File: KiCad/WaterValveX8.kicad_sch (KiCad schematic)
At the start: 89 parts, among them J10 Screw_Terminal_01x03, J2 Conn_01x03_Male, J3 Screw_Terminal_01x02, J4 Conn_01x01_Male, J5 Screw_Terminal_01x03, J6 Conn_01x04_Male, J7 Screw_Terminal_01x03, J8 Screw_Terminal_01x03, J9 Screw_Terminal_01x03, Q1 IRLML2502, Q2 IRLML2502, Q3 IRLML2502, Q4 IRLML2502, Q5 IRLML2502, Q6 IRLML2502, Q7 IRLML2502, Q8 IRLML2502, U1 L7805, U2 XIAO-ESP32-C6-SMD, U3 MT2499A

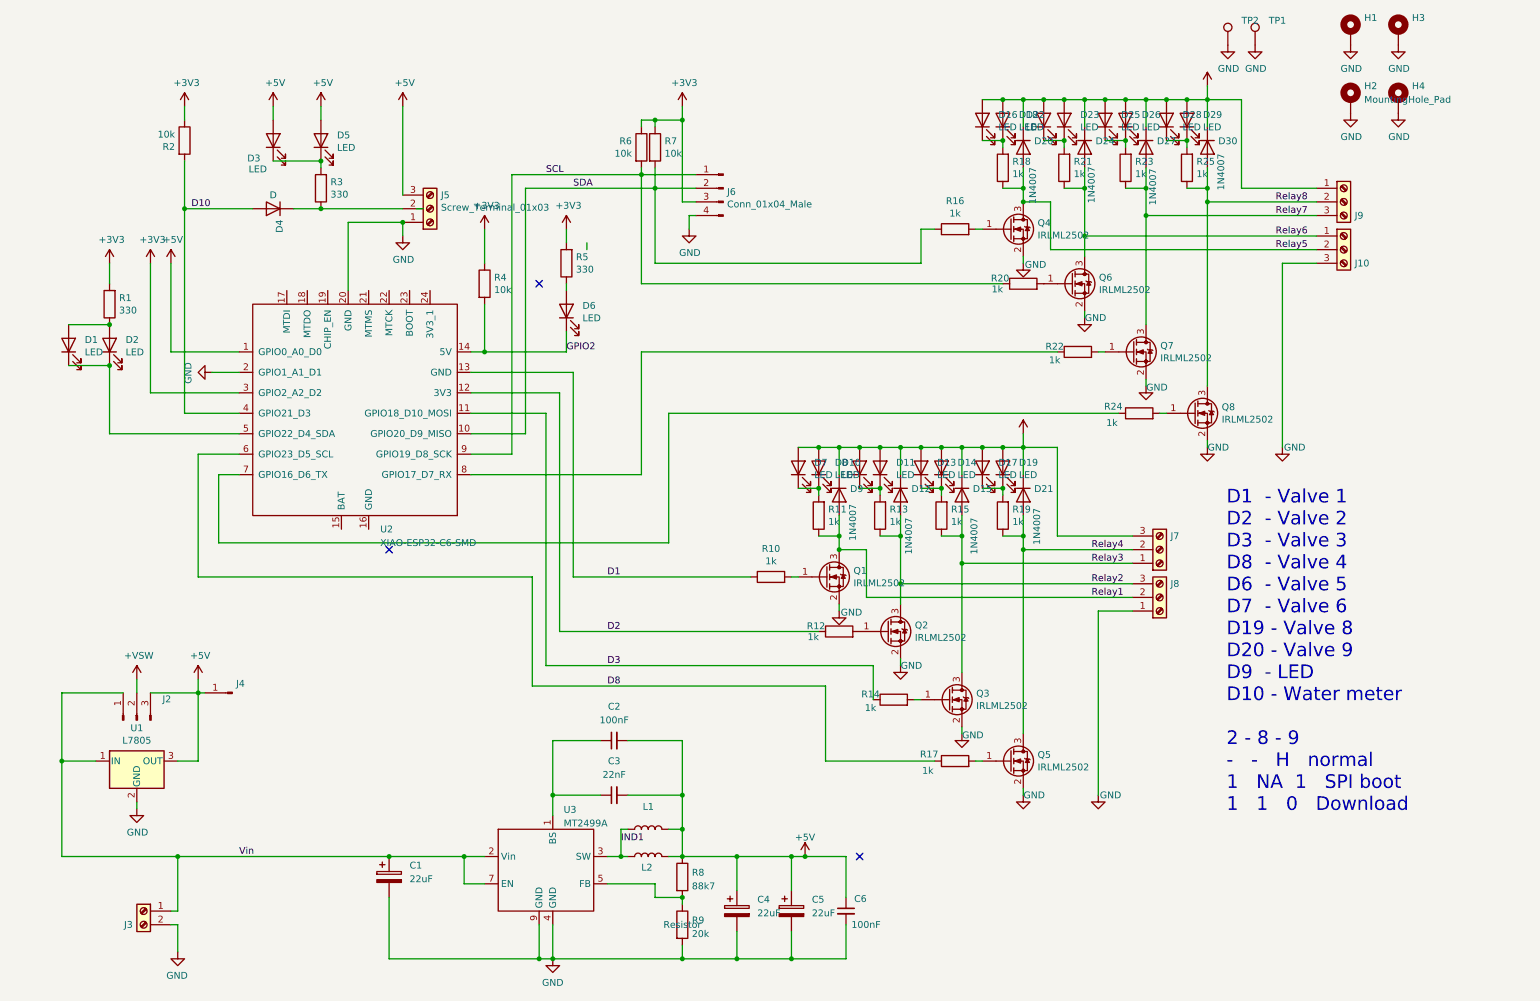
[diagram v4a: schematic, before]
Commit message: Now a esp32c6 design only. To few usable ports on c3
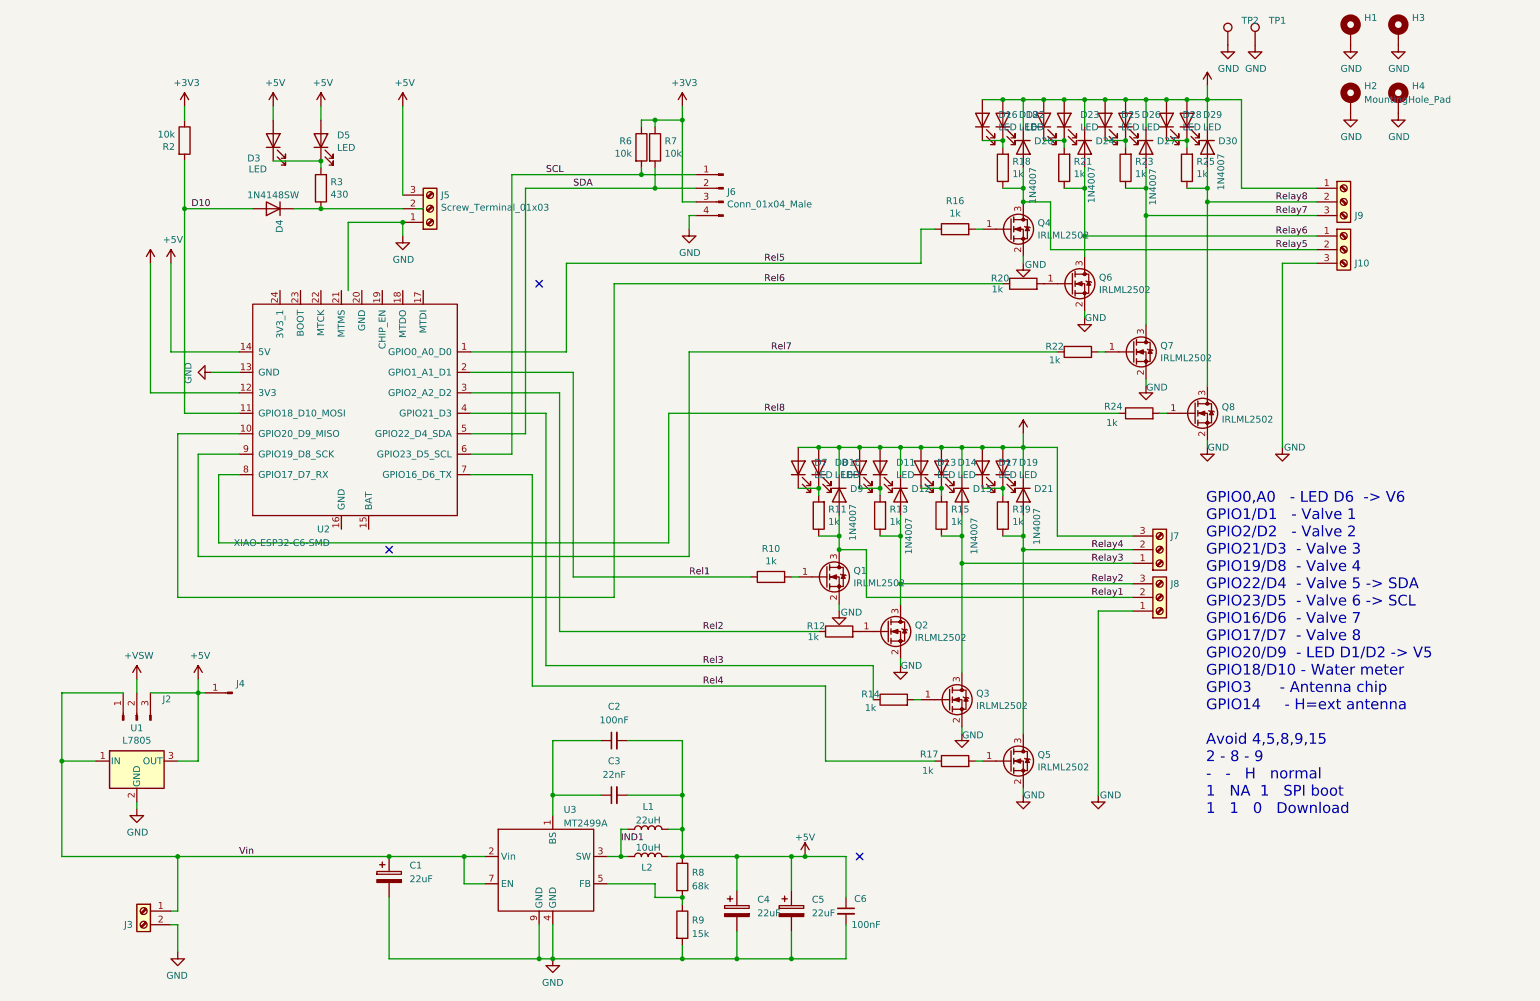
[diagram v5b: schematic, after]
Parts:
- removed D1: LED, LED_THT:LED_D3.0mm, symbol Device:LED
- removed D2, D6: LED, LED_SMD:LED_0805_2012Metric_Pad1.15x1.40mm_HandSolder, symbol Device:LED
- removed R1, R5: 330, Resistor_SMD:R_0805_2012Metric_Pad1.20x1.40mm_HandSolder, symbol Device:R
- removed R4: 10k, Resistor_SMD:R_0805_2012Metric_Pad1.20x1.40mm_HandSolder, symbol Device:R
- D4: value D -> 1N4148SW
- L1: value L -> 22uH
- L2: value L -> 10uH
- R3: value 330 -> 430
- R8: value 88k7 -> 68k
- R9: value 20k -> 15k
- U2: footprint LOCAL1:XIAO-ESP32-C3C6-SMD -> LOCAL1:XIAO-ESP32-C6-SMD
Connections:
- net GPIO2 is gone; now on net +5V: U2.14 (5V)
- net +3V3: now also U2.12 (3V3); no longer U2.3 (GPIO2_A2_D2)
- net +5V: no longer U2.1 (GPIO0_A0_D0)
- net D10: now also U2.11 (GPIO18_D10_MOSI); no longer U2.4 (GPIO21_D3)
- net GND: now also U2.13 (GND); no longer U2.2 (GPIO1_A1_D1), U2.20 (GND)
- net SCL: now also U2.6 (GPIO23_D5_SCL); no longer R20.1, U2.9 (GPIO19_D8_SCK)
- net SDA: now also U2.5 (GPIO22_D4_SDA); no longer R16.1, U2.10 (GPIO20_D9_MISO)
- net Rel4: now reaches U2.7 (GPIO16_D6_TX)
- net Rel4: now also R17.1; no longer R24.1
- net Rel7: now reaches R22.1
- net Rel7: now also U2.9 (GPIO19_D8_SCK); no longer U2.8 (GPIO17_D7_RX)
- net D1 renamed Rel1
- net Rel1: now also U2.2 (GPIO1_A1_D1); no longer U2.13 (GND)
- net D2 renamed Rel2
- net Rel2: now also U2.3 (GPIO2_A2_D2); no longer U2.12 (3V3)
- net D3 renamed Rel3
- net Rel3: now also U2.4 (GPIO21_D3); no longer U2.11 (GPIO18_D10_MOSI)
- removed net D8: R17.1, U2.6 (GPIO23_D5_SCL)
- new net Rel5: R16.1, U2.1 (GPIO0_A0_D0)
- new net Rel6: R20.1, U2.10 (GPIO20_D9_MISO)
- new net Rel8: R24.1, U2.8 (GPIO17_D7_RX)
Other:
- note added: "GPIO0,A0 - LED D6 -> V6 GPIO1/D1 - Valve 1 GPIO2/D2 - Valve 2 GPIO21/D3 - Valve 3 GPIO19/D8 - Valve 4 GPIO22/D4 - Valve 5 -> SDA GPIO23/D5 - Valve 6 -> SCL GPIO16/D6 - Valve 7 GPIO17/D7 - Valve 8 GPIO20/D9 - LED D1/D2 -> V5 GPIO18/D10 - Water meter GPIO3 - Antenna chip GPIO14 - H=ext antenna Avoid 4,5,8,9,15 2 - 8 - 9 - - H normal 1 NA 1 SPI boot 1 1 0 Download"
- note removed: "D1 - Valve 1 D2 - Valve 2 D3 - Valve 3 D8 - Valve 4 D6 - Valve 5 D7 - Valve 6 D19 - Valve 8 D20 - Valve 9 D9 - LED D10 - Water meter 2 - 8 - 9 - - H normal 1 NA 1 SPI boot 1 1 0 Download"

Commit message: Moved power in to top right
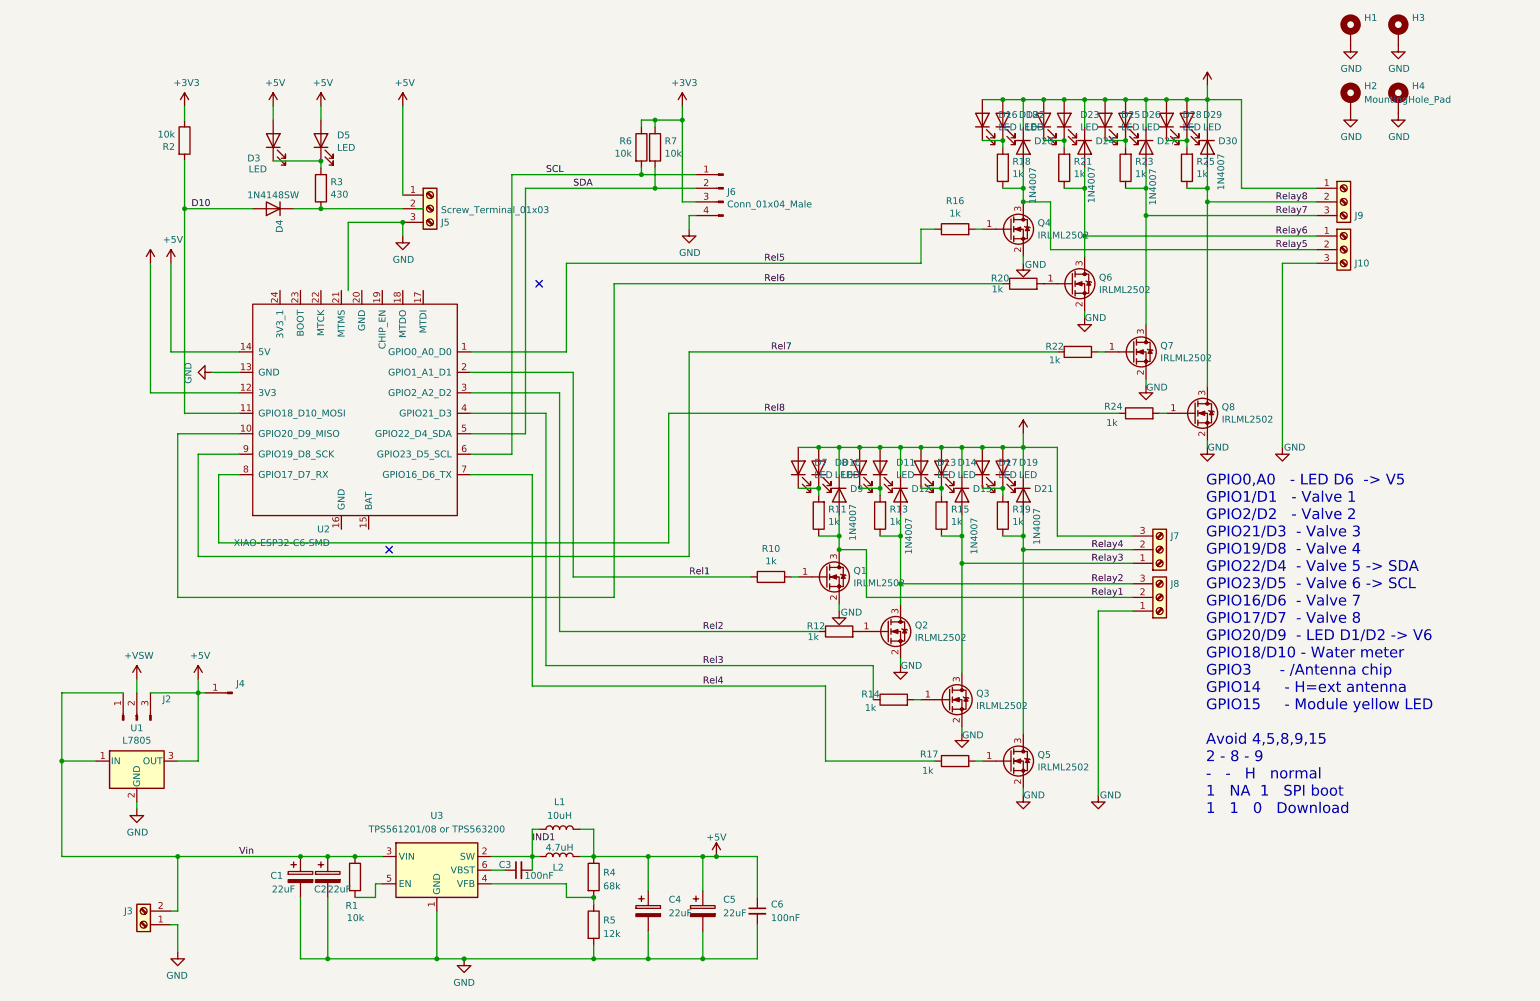
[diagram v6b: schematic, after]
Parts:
- removed C2: 100nF, Capacitor_SMD:C_0805_2012Metric_Pad1.18x1.45mm_HandSolder, symbol Device:C_Small
- removed R8: 68k, Resistor_SMD:R_0805_2012Metric_Pad1.20x1.40mm_HandSolder, symbol Device:R
- removed R9: 15k, Resistor_SMD:R_0805_2012Metric_Pad1.20x1.40mm_HandSolder, symbol Device:R
- removed TP1, TP2: TestPoint, TestPoint:TestPoint_THTPad_1.0x1.0mm_Drill0.5mm, symbol Connector:TestPoint
- removed U3: MT2499A, Package_SO:TI_SO-PowerPAD-8, symbol custom_kicad_lib_sk:MT499A
- added C2: 22uF, Capacitor_SMD:C_1206_3216Metric_Pad1.33x1.80mm_HandSolder, symbol Device:C_Polarized
- added R1: 10k, Resistor_SMD:R_0805_2012Metric_Pad1.20x1.40mm_HandSolder, symbol Device:R
- added R4: 68k, Resistor_SMD:R_0805_2012Metric_Pad1.20x1.40mm_HandSolder, symbol Device:R
- added R5: 12k, Resistor_SMD:R_0805_2012Metric_Pad1.20x1.40mm_HandSolder, symbol Device:R
- added U3: TPS561201/08 or TPS563200, Package_TO_SOT_SMD:SOT-23-6, symbol Regulator_Switching:TPS562200
- C3: value 22nF -> 100nF; JLCPCB Part# C1729 -> (none)
- L1: value 22uH -> 10uH
- L2: value 10uH -> 4.7uH; footprint Inductor_SMD:L_2512_6332Metric_Pad1.52x3.35mm_HandSolder -> Inductor_SMD:L_2010_5025Metric_Pad1.52x2.65mm_HandSolder
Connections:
- net +5V: now also J5.1 (Pin_1), R4.1; no longer C3.2, J5.3 (Pin_3)
- net GND: now also J3.1 (Pin_1), J5.3 (Pin_3), C2.2, R5.2, U3.1 (GND); no longer J3.2 (Pin_2), J5.1 (Pin_1)
- net IND1: now also C3.2, U3.2 (SW)
- net Vin: now also J3.2 (Pin_2), C2.1, R1.1, U3.3 (VIN); no longer J3.1 (Pin_1)
- net at C3.1: now also U3.6 (VBST)
- new net: R4.2, R5.1, U3.4 (VFB)
- new net: R1.2, U3.5 (EN)
- no-connect marks 3 -> 2
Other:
- note added: "GPIO0,A0 - LED D6 -> V5 GPIO1/D1 - Valve 1 GPIO2/D2 - Valve 2 GPIO21/D3 - Valve 3 GPIO19/D8 - Valve 4 GPIO22/D4 - Valve 5 -> SDA GPIO23/D5 - Valve 6 -> SCL GPIO16/D6 - Valve 7 GPIO17/D7 - Valve 8 GPIO20/D9 - LED D1/D2 -> V6 GPIO18/D10 - Water meter GPIO3 - /Antenna chip GPIO14 - H=ext antenna GPIO15 - Module yellow LED Avoid 4,5,8,9,15 2 - 8 - 9 - - H normal 1 NA 1 SPI boot 1 1 0 Download"
- note removed: "GPIO0,A0 - LED D6 -> V6 GPIO1/D1 - Valve 1 GPIO2/D2 - Valve 2 GPIO21/D3 - Valve 3 GPIO19/D8 - Valve 4 GPIO22/D4 - Valve 5 -> SDA GPIO23/D5 - Valve 6 -> SCL GPIO16/D6 - Valve 7 GPIO17/D7 - Valve 8 GPIO20/D9 - LED D1/D2 -> V5 GPIO18/D10 - Water meter GPIO3 - Antenna chip GPIO14 - H=ext antenna Avoid 4,5,8,9,15 2 - 8 - 9 - - H normal 1 NA 1 SPI boot 1 1 0 Download"
- moved on the sheet: C1, C4, C6, J3, L1, L2
